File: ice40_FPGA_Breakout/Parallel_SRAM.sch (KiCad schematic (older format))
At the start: 10 parts

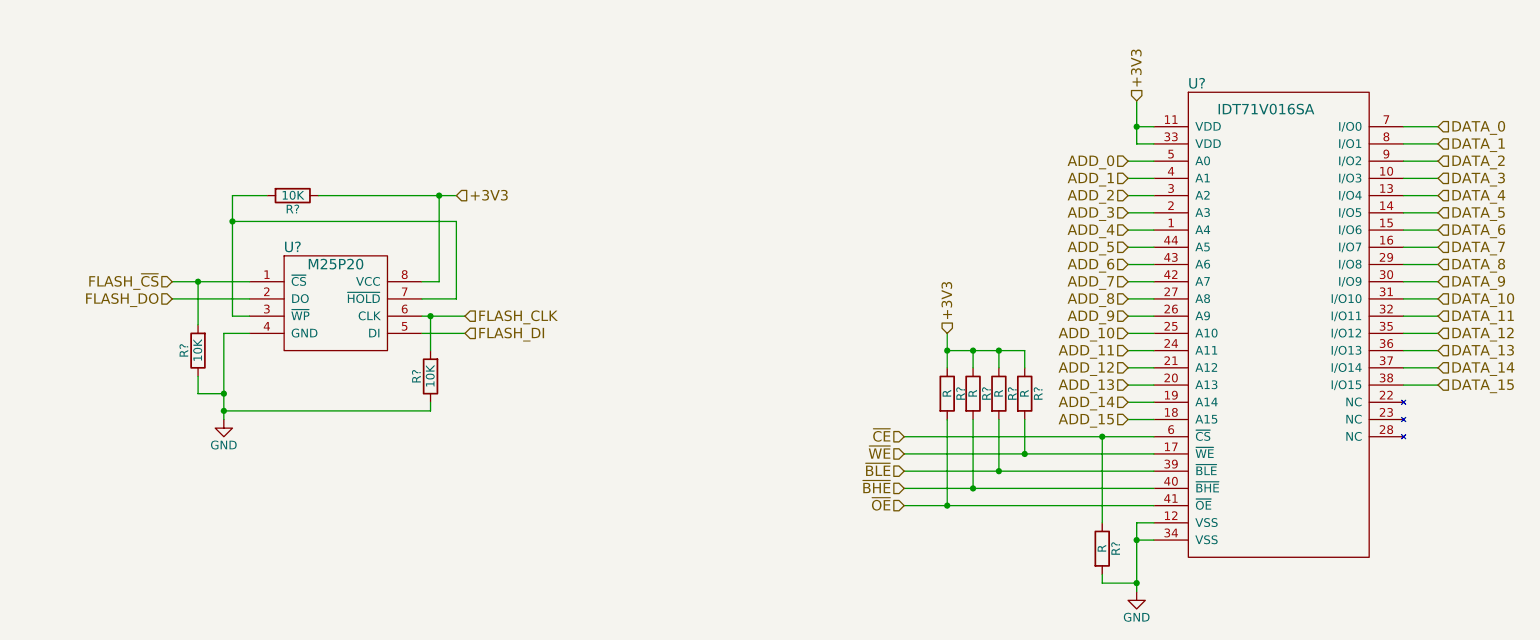
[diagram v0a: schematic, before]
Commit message: fix based on feedback and decoupluing caps added
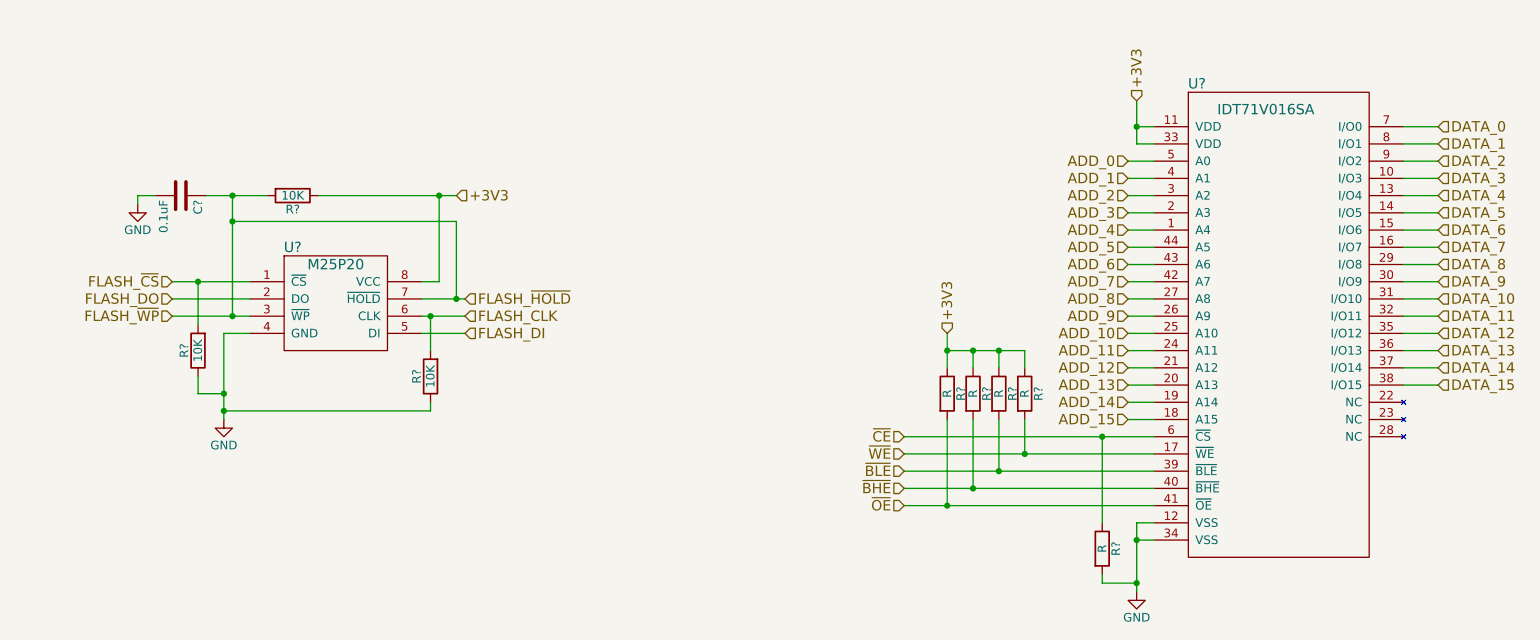
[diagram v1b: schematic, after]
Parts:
- added C?: 0.1uF, symbol C
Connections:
- net GND: now also C?.2
- net FLASH_~HOLD: now reaches R?.2, U?.3 (~WP), U?.7 (~HOLD)
- net FLASH_~HOLD: now also C?.1
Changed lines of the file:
@@
 	8350 1200 8450 1200
 Wire Wire Line
-	8350 950  8350 1100
-Wire Wire Line
-	8350 1100 8350 1200
+	8350 950  8350 1200
 Wire Wire Line
 	8450 1100 8350 1100
@@
 	8450 3400 8350 3400
 Wire Wire Line
-	8350 3400 8350 3500
-Wire Wire Line
-	8350 3500 8350 3750
-Wire Wire Line
-	8350 3750 8350 3800
+	8350 3400 8350 3800
 Wire Wire Line
 	8450 3500 8350 3500
 Connection ~ 8350 3500
 Wire Wire Line
-	7000 2900 8150 2900
-Wire Wire Line
-	8150 2900 8450 2900
-Wire Wire Line
-	7000 3000 7700 3000
-Wire Wire Line
-	7700 3000 8450 3000
-Wire Wire Line
-	7000 3100 7550 3100
-Wire Wire Line
-	7550 3100 8450 3100
-Wire Wire Line
-	7000 3200 7400 3200
-Wire Wire Line
-	7400 3200 8450 3200
-Wire Wire Line
-	7000 3300 7250 3300
-Wire Wire Line
-	7250 3300 8450 3300
+	7000 2900 8450 2900
+Wire Wire Line
+	7000 3000 8450 3000
+Wire Wire Line
+	7000 3100 8450 3100
+Wire Wire Line
+	7000 3200 8450 3200
+Wire Wire Line
+	7000 3300 8450 3300
 Wire Wire Line
 	8150 3400 8150 2900
@@
 	7700 2400 7700 2500
 Wire Wire Line
-	7250 2400 7400 2400
-Wire Wire Line
-	7400 2400 7550 2400
-Wire Wire Line
-	7550 2400 7700 2400
-Wire Wire Line
-	7250 2300 7250 2400
-Wire Wire Line
-	7250 2400 7250 2500
+	7250 2400 7700 2400
+Wire Wire Line
+	7250 2300 7250 2500
 Connection ~ 7250 2400
 Wire Wire Line
@@
 	9900 2600 10100 2600
 Wire Wire Line
-	4200 2100 4400 2100
+	4200 2100 4450 2100
 Wire Wire Line
 	4400 2100 4400 1650
 Wire Wire Line
-	3100 1500 3100 1650
-Wire Wire Line
-	3100 1650 3100 2200
-Wire Wire Line
-	3100 2200 3200 2200
+	3100 1500 3100 2200
+Wire Wire Line
+	2750 2200 3200 2200
 Wire Wire Line
 	3200 2300 3050 2300
 Wire Wire Line
-	3050 2300 3050 2650
-Wire Wire Line
-	3050 2650 3050 2750
-Wire Wire Line
-	3050 2750 3050 2800
+	3050 2300 3050 2800
 Wire Wire Line
 	4300 2000 4200 2000
 Wire Wire Line
-	2750 2000 2900 2000
-Wire Wire Line
-	2900 2000 3200 2000
+	2750 2000 3200 2000
 Wire Wire Line
 	3200 2100 2750 2100
 Wire Wire Line
-	4200 2200 4250 2200
-Wire Wire Line
-	4250 2200 4450 2200
+	4200 2200 4450 2200
 Wire Wire Line
 	4200 2300 4450 2300
 Wire Wire Line
-	3600 1500 4300 1500
-Wire Wire Line
-	4300 1500 4400 1500
+	3600 1500 4400 1500
 Wire Wire Line
 	4400 1650 3100 1650
@@
 	4300 1500 4300 2000
 Wire Wire Line
-	3100 1500 3300 1500
+	2950 1500 3300 1500
 Connection ~ 3100 1650
 Connection ~ 4300 1500
@@
 	4250 2750 3050 2750
 Connection ~ 3050 2750
+Text HLabel 2750 2200 0    60   Input ~ 0
+FLASH_~WP
+Text HLabel 4450 2100 2    60   Input ~ 0
+FLASH_~HOLD
+Connection ~ 4400 2100
+Connection ~ 3100 2200
+$Comp
+L C C?
+U 1 1 5A60AEA1
+P 2800 1500
+F 0 "C?" H 2825 1600 50  0000 L CNN
+F 1 "0.1uF" H 2825 1400 50  0000 L CNN
+F 2 "" H 2838 1350 50  0001 C CNN
+F 3 "" H 2800 1500 50  0001 C CNN
+	1    2800 1500
+	0    1    1    0
+$EndComp
+Connection ~ 3100 1500
+Wire Wire Line
+	2650 1500 2550 1500
+Wire Wire Line
+	2550 1500 2550 1550
+$Comp
+L GND #PWR?
+U 1 1 5A60B07E
+P 2550 1550
+F 0 "#PWR?" H 2550 1300 50  0001 C CNN
+F 1 "GND" H 2550 1400 50  0000 C CNN
+F 2 "" H 2550 1550 50  0001 C CNN
+F 3 "" H 2550 1550 50  0001 C CNN
+	1    2550 1550
+	1    0    0    -1
+$EndComp
 $EndSCHEMATC

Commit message: post review fix
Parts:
- added R? (x2): 10K, symbol R
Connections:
- net +3V3: now also R?.1, R?.1
- net FLASH_~CS: now also R?.2
- net FLASH_~HOLD: now also R?.2
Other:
- moved on the sheet: C?, R?
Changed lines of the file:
@@
 L R R?
 U 1 1 5A55FF49
-P 3450 1500
-F 0 "R?" V 3530 1500 50  0000 C CNN
-F 1 "10K" V 3450 1500 50  0000 C CNN
-F 2 "" V 3380 1500 50  0001 C CNN
-F 3 "" H 3450 1500 50  0001 C CNN
-	1    3450 1500
+P 3450 1100
+F 0 "R?" V 3530 1100 50  0000 C CNN
+F 1 "10K" V 3450 1100 50  0000 C CNN
+F 2 "" V 3380 1100 50  0001 C CNN
+F 3 "" H 3450 1100 50  0001 C CNN
+	1    3450 1100
 	0    1    1    0
 $EndComp
-Text HLabel 4400 1500 2    60   Input ~ 0
+Text HLabel 4400 1100 2    60   Input ~ 0
 +3V3
 $Comp
@@
 	1    0    0    -1
 $EndComp
-Text HLabel 4450 2200 2    60   Input ~ 0
+Text HLabel 4550 2200 2    60   Input ~ 0
 FLASH_CLK
-Text HLabel 4450 2300 2    60   Input ~ 0
+Text HLabel 4550 2300 2    60   Input ~ 0
 FLASH_DI
-Text HLabel 2750 2100 0    60   Input ~ 0
+Text HLabel 2600 2100 0    60   Input ~ 0
 FLASH_DO
-Text HLabel 2750 2000 0    60   Input ~ 0
+Text HLabel 2600 2000 0    60   Input ~ 0
 FLASH_~CS
 Wire Wire Line
 	8350 1200 8450 1200
 Wire Wire Line
-	8350 950  8350 1200
+	8350 950  8350 1100
+Wire Wire Line
+	8350 1100 8350 1200
 Wire Wire Line
 	8450 1100 8350 1100
@@
 	8450 3400 8350 3400
 Wire Wire Line
-	8350 3400 8350 3800
+	8350 3400 8350 3500
+Wire Wire Line
+	8350 3500 8350 3750
+Wire Wire Line
+	8350 3750 8350 3800
 Wire Wire Line
 	8450 3500 8350 3500
 Connection ~ 8350 3500
 Wire Wire Line
-	7000 2900 8450 2900
-Wire Wire Line
-	7000 3000 8450 3000
-Wire Wire Line
-	7000 3100 8450 3100
-Wire Wire Line
-	7000 3200 8450 3200
-Wire Wire Line
-	7000 3300 8450 3300
+	7000 2900 8150 2900
+Wire Wire Line
+	8150 2900 8450 2900
+Wire Wire Line
+	7000 3000 7700 3000
+Wire Wire Line
+	7700 3000 8450 3000
+Wire Wire Line
+	7000 3100 7550 3100
+Wire Wire Line
+	7550 3100 8450 3100
+Wire Wire Line
+	7000 3200 7400 3200
+Wire Wire Line
+	7400 3200 8450 3200
+Wire Wire Line
+	7000 3300 7250 3300
+Wire Wire Line
+	7250 3300 8450 3300
 Wire Wire Line
 	8150 3400 8150 2900
@@
 	7700 2400 7700 2500
 Wire Wire Line
-	7250 2400 7700 2400
-Wire Wire Line
-	7250 2300 7250 2500
+	7250 2400 7400 2400
+Wire Wire Line
+	7400 2400 7550 2400
+Wire Wire Line
+	7550 2400 7700 2400
+Wire Wire Line
+	7250 2300 7250 2400
+Wire Wire Line
+	7250 2400 7250 2500
 Connection ~ 7250 2400
 Wire Wire Line
@@
 	9900 2600 10100 2600
 Wire Wire Line
-	4200 2100 4450 2100
-Wire Wire Line
-	4400 2100 4400 1650
-Wire Wire Line
-	3100 1500 3100 2200
-Wire Wire Line
-	2750 2200 3200 2200
+	4200 2100 4400 2100
+Wire Wire Line
+	4400 2100 4550 2100
+Wire Wire Line
+	4400 2100 4400 1250
+Wire Wire Line
+	3000 1100 3000 1250
+Wire Wire Line
+	3000 1250 3000 1450
+Wire Wire Line
+	3000 1450 3000 2200
+Wire Wire Line
+	2600 2200 3000 2200
+Wire Wire Line
+	3000 2200 3200 2200
 Wire Wire Line
 	3200 2300 3050 2300
 Wire Wire Line
-	3050 2300 3050 2800
+	3050 2300 3050 2650
+Wire Wire Line
+	3050 2650 3050 2750
+Wire Wire Line
+	3050 2750 3050 2800
 Wire Wire Line
 	4300 2000 4200 2000
 Wire Wire Line
-	2750 2000 3200 2000
-Wire Wire Line
-	3200 2100 2750 2100
-Wire Wire Line
-	4200 2200 4450 2200
-Wire Wire Line
-	4200 2300 4450 2300
-Wire Wire Line
-	3600 1500 4400 1500
-Wire Wire Line
-	4400 1650 3100 1650
-Wire Wire Line
-	4300 1500 4300 2000
-Wire Wire Line
-	2950 1500 3300 1500
-Connection ~ 3100 1650
-Connection ~ 4300 1500
+	2600 2000 2900 2000
+Wire Wire Line
+	2900 2000 3150 2000
+Wire Wire Line
+	3150 2000 3200 2000
+Wire Wire Line
+	3200 2100 2600 2100
+Wire Wire Line
+	4200 2200 4250 2200
+Wire Wire Line
+	4250 2200 4550 2200
+Wire Wire Line
+	4200 2300 4550 2300
+Wire Wire Line
+	3600 1100 3750 1100
+Wire Wire Line
+	3750 1100 4300 1100
+Wire Wire Line
+	4300 1100 4400 1100
+Wire Wire Line
+	4400 1250 3000 1250
+Wire Wire Line
+	4300 1100 4300 2000
+Wire Wire Line
+	2850 1100 3000 1100
+Wire Wire Line
+	3000 1100 3300 1100
+Connection ~ 3000 1250
+Connection ~ 4300 1100
 $Comp
 L R R?
@@
 	4250 2750 3050 2750
 Connection ~ 3050 2750
-Text HLabel 2750 2200 0    60   Input ~ 0
+Text HLabel 2600 2200 0    60   Input ~ 0
 FLASH_~WP
-Text HLabel 4450 2100 2    60   Input ~ 0
+Text HLabel 4550 2100 2    60   Input ~ 0
 FLASH_~HOLD
 Connection ~ 4400 2100
-Connection ~ 3100 2200
+Connection ~ 3000 2200
 $Comp
 L C C?
 U 1 1 5A60AEA1
-P 2800 1500
-F 0 "C?" H 2825 1600 50  0000 L CNN
-F 1 "0.1uF" H 2825 1400 50  0000 L CNN
-F 2 "" H 2838 1350 50  0001 C CNN
-F 3 "" H 2800 1500 50  0001 C CNN
-	1    2800 1500
+P 2700 1100
+F 0 "C?" H 2725 1200 50  0000 L CNN
+F 1 "0.1uF" H 2725 1000 50  0000 L CNN
+F 2 "" H 2738 950 50  0001 C CNN
+F 3 "" H 2700 1100 50  0001 C CNN
+	1    2700 1100
 	0    1    1    0
 $EndComp
-Connection ~ 3100 1500
-Wire Wire Line
-	2650 1500 2550 1500
-Wire Wire Line
-	2550 1500 2550 1550
+Connection ~ 3000 1100
+Wire Wire Line
+	2550 1100 2450 1100
+Wire Wire Line
+	2450 1100 2450 1250
 $Comp
 L GND #PWR?
 U 1 1 5A60B07E
-P 2550 1550
-F 0 "#PWR?" H 2550 1300 50  0001 C CNN
-F 1 "GND" H 2550 1400 50  0000 C CNN
-F 2 "" H 2550 1550 50  0001 C CNN
-F 3 "" H 2550 1550 50  0001 C CNN
-	1    2550 1550
+P 2450 1250
+F 0 "#PWR?" H 2450 1000 50  0001 C CNN
+F 1 "GND" H 2450 1100 50  0000 C CNN
+F 2 "" H 2450 1250 50  0001 C CNN
+F 3 "" H 2450 1250 50  0001 C CNN
+	1    2450 1250
 	1    0    0    -1
 $EndComp
+$Comp
+L R R?
+U 1 1 5A6077BD
+P 3450 1450
+F 0 "R?" V 3530 1450 50  0000 C CNN
+F 1 "10K" V 3450 1450 50  0000 C CNN
+F 2 "" V 3380 1450 50  0001 C CNN
+F 3 "" H 3450 1450 50  0001 C CNN
+	1    3450 1450
+	0    1    1    0
+$EndComp
+$Comp
+L R R?
+U 1 1 5A60780F
+P 3450 1600
+F 0 "R?" V 3530 1600 50  0000 C CNN
+F 1 "10K" V 3450 1600 50  0000 C CNN
+F 2 "" V 3380 1600 50  0001 C CNN
+F 3 "" H 3450 1600 50  0001 C CNN
+	1    3450 1600
+	0    1    1    0
+$EndComp
+Wire Wire Line
+	3600 1450 3750 1450
+Wire Wire Line
+	3750 1100 3750 1450
+Wire Wire Line
+	3750 1450 3750 1600
+Connection ~ 3750 1100
+Wire Wire Line
+	3750 1600 3600 1600
+Connection ~ 3750 1450
+Wire Wire Line
+	3300 1600 3150 1600
+Wire Wire Line
+	3150 1600 3150 2000
+Connection ~ 3150 2000
+Wire Wire Line
+	3300 1450 3000 1450
+Connection ~ 3000 1450
 $EndSCHEMATC

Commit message: Component Annotated and R/C/Conn/TP CVPCB mapping
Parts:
- R105, R106, R107, R108, R109: renamed from R?; value R -> 10K
- gave numbers to parts that had none: 8
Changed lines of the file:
@@
 $EndDescr
 $Comp
-L IDT71V016SA U?
+L IDT71V016SA U4
 U 1 1 5A55C80D
 P 9150 900
-F 0 "U?" H 8700 950 60  0000 C CNN
+F 0 "U4" H 8700 950 60  0000 C CNN
 F 1 "IDT71V016SA" H 9100 800 60  0000 C CNN
 F 2 "" H 9150 900 60  0001 C CNN
@@
 ~OE
 $Comp
-L GND #PWR?
+L GND #PWR019
 U 1 1 5A55CACE
 P 8350 3800
-F 0 "#PWR?" H 8350 3550 50  0001 C CNN
+F 0 "#PWR019" H 8350 3550 50  0001 C CNN
 F 1 "GND" H 8350 3650 50  0000 C CNN
 F 2 "" H 8350 3800 50  0001 C CNN
@@
 $EndComp
 $Comp
-L R R?
+L R R109
 U 1 1 5A55CAEB
 P 8150 3550
-F 0 "R?" V 8230 3550 50  0000 C CNN
-F 1 "R" V 8150 3550 50  0000 C CNN
+F 0 "R109" V 8230 3550 50  0000 C CNN
+F 1 "10K" V 8150 3550 50  0000 C CNN
 F 2 "" V 8080 3550 50  0001 C CNN
 F 3 "" H 8150 3550 50  0001 C CNN
@@
 $EndComp
 $Comp
-L R R?
+L R R105
 U 1 1 5A55CB26
 P 7250 2650
-F 0 "R?" V 7330 2650 50  0000 C CNN
-F 1 "R" V 7250 2650 50  0000 C CNN
+F 0 "R105" V 7330 2650 50  0000 C CNN
+F 1 "10K" V 7250 2650 50  0000 C CNN
 F 2 "" V 7180 2650 50  0001 C CNN
 F 3 "" H 7250 2650 50  0001 C CNN
@@
 $EndComp
 $Comp
-L R R?
+L R R106
 U 1 1 5A55CB43
 P 7400 2650
-F 0 "R?" V 7480 2650 50  0000 C CNN
-F 1 "R" V 7400 2650 50  0000 C CNN
+F 0 "R106" V 7480 2650 50  0000 C CNN
+F 1 "10K" V 7400 2650 50  0000 C CNN
 F 2 "" V 7330 2650 50  0001 C CNN
 F 3 "" H 7400 2650 50  0001 C CNN
@@
 $EndComp
 $Comp
-L R R?
+L R R107
 U 1 1 5A55CB63
 P 7550 2650
-F 0 "R?" V 7630 2650 50  0000 C CNN
-F 1 "R" V 7550 2650 50  0000 C CNN
+F 0 "R107" V 7630 2650 50  0000 C CNN
+F 1 "10K" V 7550 2650 50  0000 C CNN
 F 2 "" V 7480 2650 50  0001 C CNN
 F 3 "" H 7550 2650 50  0001 C CNN
@@
 $EndComp
 $Comp
-L R R?
+L R R108
 U 1 1 5A55CB8C
 P 7700 2650
-F 0 "R?" V 7780 2650 50  0000 C CNN
-F 1 "R" V 7700 2650 50  0000 C CNN
+F 0 "R108" V 7780 2650 50  0000 C CNN
+F 1 "10K" V 7700 2650 50  0000 C CNN
 F 2 "" V 7630 2650 50  0001 C CNN
 F 3 "" H 7700 2650 50  0001 C CNN
@@
 DATA_15
 $Comp
-L M25P20 U?
+L M25P20 U3
 U 1 1 5A55FCF8
 P 3700 1850
-F 0 "U?" H 3450 1900 60  0000 C CNN
+F 0 "U3" H 3450 1900 60  0000 C CNN
 F 1 "M25P20" H 3700 1800 60  0000 C CNN
 F 2 "" H 3700 1900 60  0001 C CNN
@@
 $EndComp
 $Comp
-L R R?
+L R R101
 U 1 1 5A55FF49
 P 3450 1100
-F 0 "R?" V 3530 1100 50  0000 C CNN
+F 0 "R101" V 3530 1100 50  0000 C CNN
 F 1 "10K" V 3450 1100 50  0000 C CNN
 F 2 "" V 3380 1100 50  0001 C CNN
@@
 +3V3
 $Comp
-L GND #PWR?
+L GND #PWR020
 U 1 1 5A56030B
 P 3050 2800
-F 0 "#PWR?" H 3050 2550 50  0001 C CNN
+F 0 "#PWR020" H 3050 2550 50  0001 C CNN
 F 1 "GND" H 3050 2650 50  0000 C CNN
 F 2 "" H 3050 2800 50  0001 C CNN
@@
 	8350 1200 8450 1200
 Wire Wire Line
-	8350 950  8350 1100
-Wire Wire Line
-	8350 1100 8350 1200
+	8350 950  8350 1200
 Wire Wire Line
 	8450 1100 8350 1100
@@
 	8450 3400 8350 3400
 Wire Wire Line
-	8350 3400 8350 3500
-Wire Wire Line
-	8350 3500 8350 3750
-Wire Wire Line
-	8350 3750 8350 3800
+	8350 3400 8350 3800
 Wire Wire Line
 	8450 3500 8350 3500
 Connection ~ 8350 3500
 Wire Wire Line
-	7000 2900 8150 2900
-Wire Wire Line
-	8150 2900 8450 2900
-Wire Wire Line
-	7000 3000 7700 3000
-Wire Wire Line
-	7700 3000 8450 3000
-Wire Wire Line
-	7000 3100 7550 3100
-Wire Wire Line
-	7550 3100 8450 3100
-Wire Wire Line
-	7000 3200 7400 3200
-Wire Wire Line
-	7400 3200 8450 3200
-Wire Wire Line
-	7000 3300 7250 3300
-Wire Wire Line
-	7250 3300 8450 3300
+	7000 2900 8450 2900
+Wire Wire Line
+	7000 3000 8450 3000
+Wire Wire Line
+	7000 3100 8450 3100
+Wire Wire Line
+	7000 3200 8450 3200
+Wire Wire Line
+	7000 3300 8450 3300
 Wire Wire Line
 	8150 3400 8150 2900
@@
 	7700 2400 7700 2500
 Wire Wire Line
-	7250 2400 7400 2400
-Wire Wire Line
-	7400 2400 7550 2400
-Wire Wire Line
-	7550 2400 7700 2400
-Wire Wire Line
-	7250 2300 7250 2400
-Wire Wire Line
-	7250 2400 7250 2500
+	7250 2400 7700 2400
+Wire Wire Line
+	7250 2300 7250 2500
 Connection ~ 7250 2400
 Wire Wire Line
@@
 	9900 2600 10100 2600
 Wire Wire Line
-	4200 2100 4400 2100
-Wire Wire Line
-	4400 2100 4550 2100
+	4200 2100 4550 2100
 Wire Wire Line
 	4400 2100 4400 1250
 Wire Wire Line
-	3000 1100 3000 1250
-Wire Wire Line
-	3000 1250 3000 1450
-Wire Wire Line
-	3000 1450 3000 2200
-Wire Wire Line
-	2600 2200 3000 2200
-Wire Wire Line
-	3000 2200 3200 2200
+	3000 1100 3000 2200
+Wire Wire Line
+	2600 2200 3200 2200
 Wire Wire Line
 	3200 2300 3050 2300
 Wire Wire Line
-	3050 2300 3050 2650
-Wire Wire Line
-	3050 2650 3050 2750
-Wire Wire Line
-	3050 2750 3050 2800
+	3050 2300 3050 2800
 Wire Wire Line
 	4300 2000 4200 2000
 Wire Wire Line
-	2600 2000 2900 2000
-Wire Wire Line
-	2900 2000 3150 2000
-Wire Wire Line
-	3150 2000 3200 2000
+	2600 2000 3200 2000
 Wire Wire Line
 	3200 2100 2600 2100
 Wire Wire Line
-	4200 2200 4250 2200
-Wire Wire Line
-	4250 2200 4550 2200
+	4200 2200 4550 2200
 Wire Wire Line
 	4200 2300 4550 2300
 Wire Wire Line
-	3600 1100 3750 1100
-Wire Wire Line
-	3750 1100 4300 1100
-Wire Wire Line
-	4300 1100 4400 1100
+	3600 1100 4400 1100
 Wire Wire Line
 	4400 1250 3000 1250
@@
 	4300 1100 4300 2000
 Wire Wire Line
-	2850 1100 3000 1100
-Wire Wire Line
-	3000 1100 3300 1100
+	2850 1100 3300 1100
 Connection ~ 3000 1250
 Connection ~ 4300 1100
 $Comp
-L R R?
+L R R100
 U 1 1 5A560B5E
 P 2900 2400
-F 0 "R?" V 2980 2400 50  0000 C CNN
+F 0 "R100" V 2980 2400 50  0000 C CNN
 F 1 "10K" V 2900 2400 50  0000 C CNN
 F 2 "" V 2830 2400 50  0001 C CNN
@@
 Connection ~ 3050 2650
 $Comp
-L R R?
+L R R104
 U 1 1 5A5D39B2
 P 4250 2550
-F 0 "R?" V 4330 2550 50  0000 C CNN
+F 0 "R104" V 4330 2550 50  0000 C CNN
 F 1 "10K" V 4250 2550 50  0000 C CNN
 F 2 "" V 4180 2550 50  0001 C CNN
@@
 Connection ~ 3000 2200
 $Comp
-L C C?
+L C C21
 U 1 1 5A60AEA1
 P 2700 1100
-F 0 "C?" H 2725 1200 50  0000 L CNN
+F 0 "C21" H 2725 1200 50  0000 L CNN
 F 1 "0.1uF" H 2725 1000 50  0000 L CNN
 F 2 "" H 2738 950 50  0001 C CNN
@@
 	2450 1100 2450 1250
 $Comp
-L GND #PWR?
+L GND #PWR021
 U 1 1 5A60B07E
 P 2450 1250
-F 0 "#PWR?" H 2450 1000 50  0001 C CNN
+F 0 "#PWR021" H 2450 1000 50  0001 C CNN
 F 1 "GND" H 2450 1100 50  0000 C CNN
 F 2 "" H 2450 1250 50  0001 C CNN
@@
 $EndComp
 $Comp
-L R R?
+L R R102
 U 1 1 5A6077BD
 P 3450 1450
-F 0 "R?" V 3530 1450 50  0000 C CNN
+F 0 "R102" V 3530 1450 50  0000 C CNN
 F 1 "10K" V 3450 1450 50  0000 C CNN
 F 2 "" V 3380 1450 50  0001 C CNN
@@
 $EndComp
 $Comp
-L R R?
+L R R103
 U 1 1 5A60780F
 P 3450 1600
-F 0 "R?" V 3530 1600 50  0000 C CNN
+F 0 "R103" V 3530 1600 50  0000 C CNN
 F 1 "10K" V 3450 1600 50  0000 C CNN
 F 2 "" V 3380 1600 50  0001 C CNN
@@
 	3600 1450 3750 1450
 Wire Wire Line
-	3750 1100 3750 1450
-Wire Wire Line
-	3750 1450 3750 1600
+	3750 1100 3750 1600
 Connection ~ 3750 1100
 Wire Wire Line
